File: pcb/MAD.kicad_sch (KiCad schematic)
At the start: 48 parts, among them J1 Conn_01x06_Pin, J2 Conn_01x06_Socket, Q1 AO3416A, Q10 AO3419A, Q11 AO3416A, Q12 AO3416A, Q2 AO3419A, Q3 AO3416A, Q4 AO3419A, Q5 AO3416A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

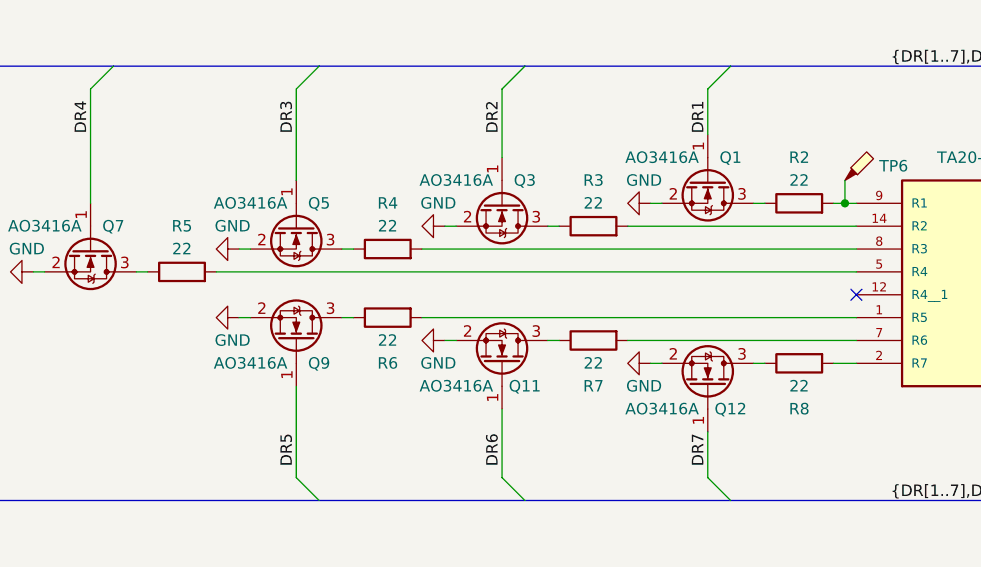
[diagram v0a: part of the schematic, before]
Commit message: Optimize resistor values
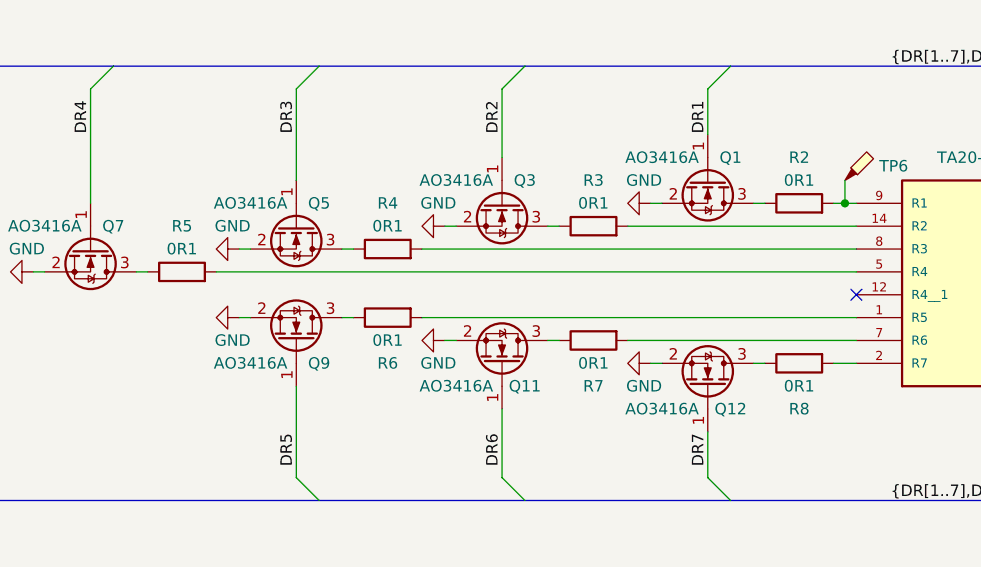
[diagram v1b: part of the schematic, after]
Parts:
- R2, R3, R4, R5, R6, R7, R8: value 22 -> 0R1
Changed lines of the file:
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@@
       (effects (font (size 1.27 1.27)))
     )
-    (property "Value" "22" (at 196.85 114.3 90)
+    (property "Value" "0R1" (at 196.85 114.3 90)
       (effects (font (size 1.27 1.27)))
     )
@@
       (effects (font (size 1.27 1.27)))
     )
-    (property "Value" "22" (at 173.99 111.76 90)
+    (property "Value" "0R1" (at 173.99 111.76 90)
       (effects (font (size 1.27 1.27)))
     )
@@
       (effects (font (size 1.27 1.27)))
     )
-    (property "Value" "22" (at 196.85 91.44 90)
+    (property "Value" "0R1" (at 196.85 91.44 90)
       (effects (font (size 1.27 1.27)))
     )
@@
       (effects (font (size 1.27 1.27)))
     )
-    (property "Value" "22" (at 151.13 109.22 90)
+    (property "Value" "0R1" (at 151.13 109.22 90)
       (effects (font (size 1.27 1.27)))
     )
@@
       (effects (font (size 1.27 1.27)))
     )
-    (property "Value" "22" (at 128.27 99.06 90)
+    (property "Value" "0R1" (at 128.27 99.06 90)
       (effects (font (size 1.27 1.27)))
     )
@@
       (effects (font (size 1.27 1.27)))
     )
-    (property "Value" "22" (at 151.13 96.52 90)
+    (property "Value" "0R1" (at 151.13 96.52 90)
       (effects (font (size 1.27 1.27)))
     )
@@
       (effects (font (size 1.27 1.27)))
     )
-    (property "Value" "22" (at 173.99 93.98 90)
-      (effects (font (size 1.27 1.27)))
-    )
+    (property "Value" "0R1" (at 173.99 93.98 90)
+      (effects (font (size 1.27 1.27)))
+    )

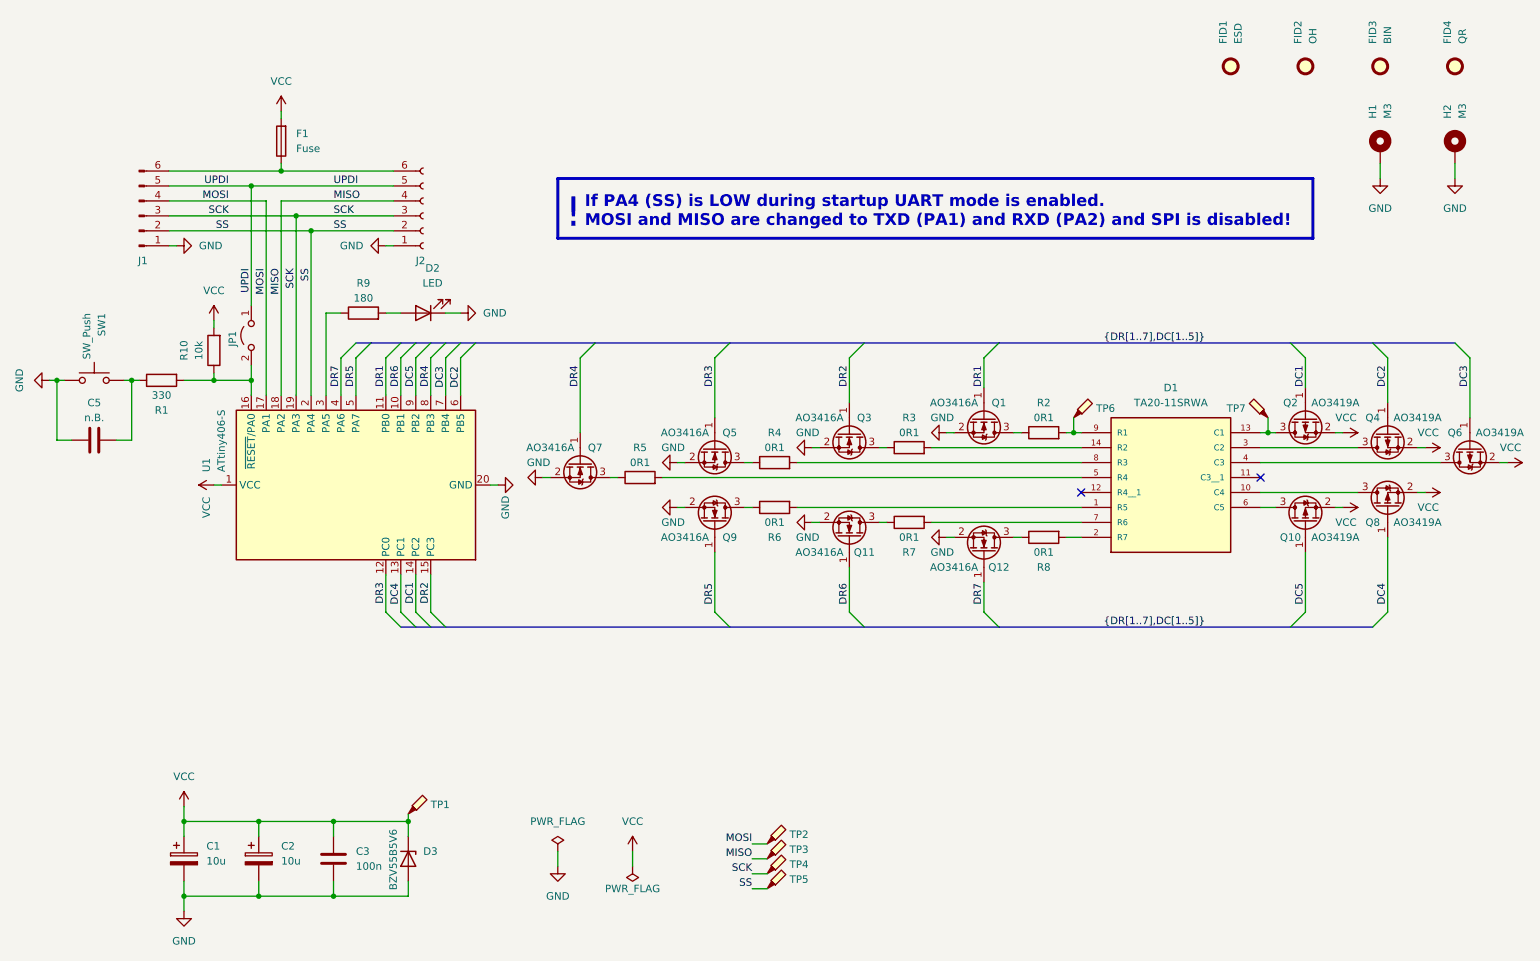
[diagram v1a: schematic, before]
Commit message: Change SPI-Bus names
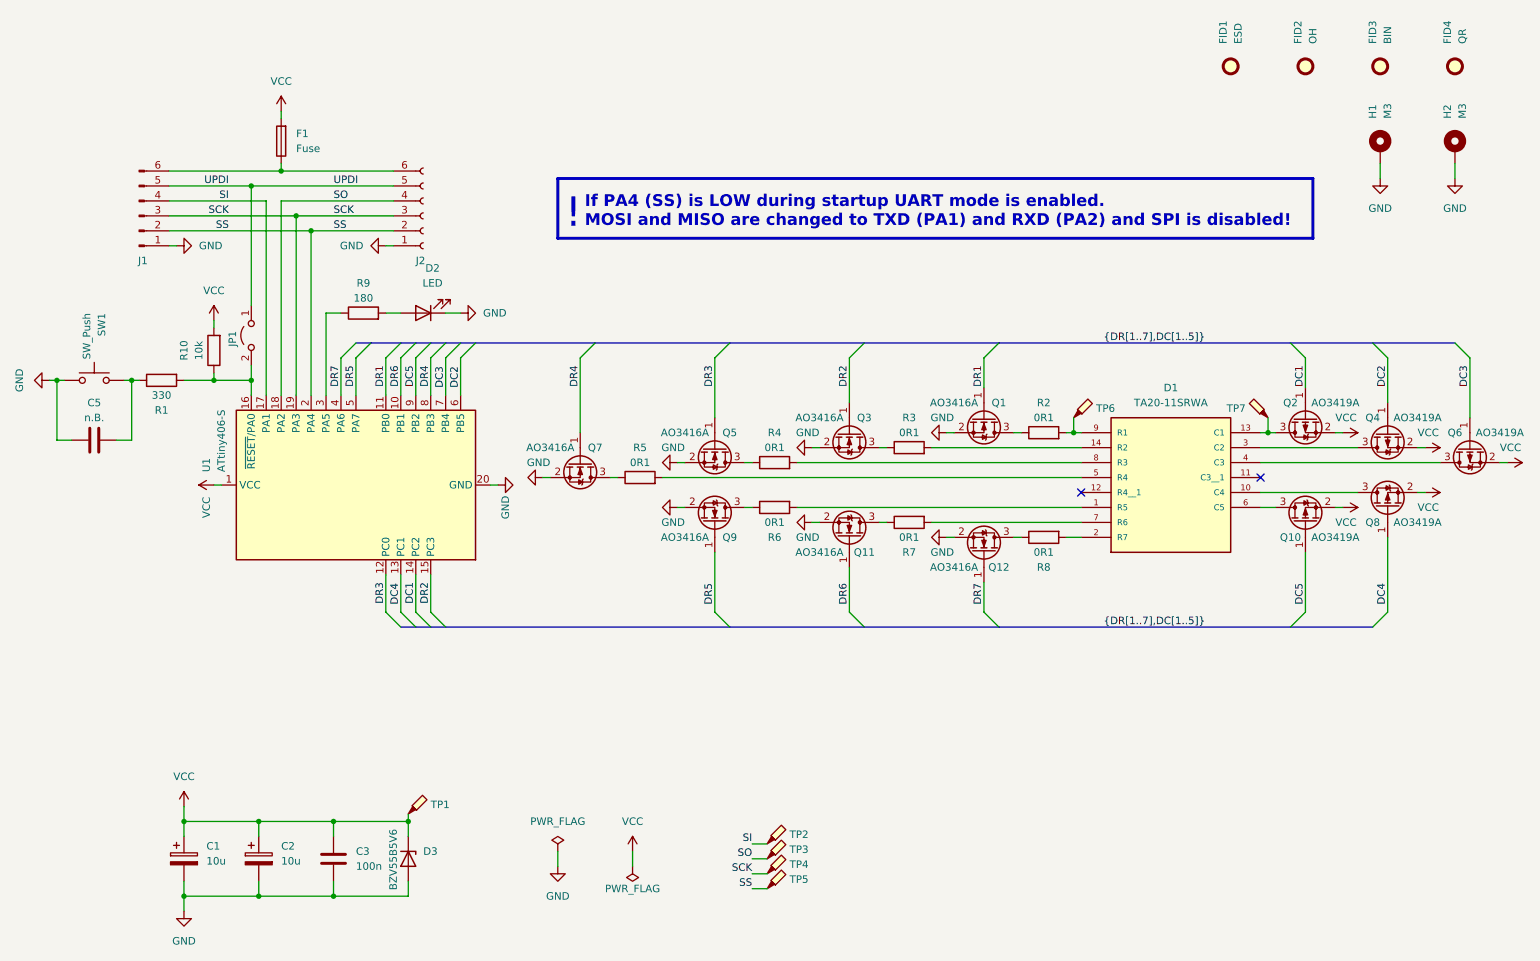
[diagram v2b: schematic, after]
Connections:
- net MISO renamed SO
- net MOSI renamed SI
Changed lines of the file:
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@@
     (effects (font (size 1.27 1.27)) (justify left bottom))
   )
-  (label "MOSI" (at 147.32 163.83 180) (fields_autoplaced)
+  (label "SI" (at 147.32 163.83 180) (fields_autoplaced)
     (effects (font (size 1.27 1.27)) (justify right bottom))
   )
   (label "DR6" (at 87.63 82.55 270) (fields_autoplaced)
-    (effects (font (size 1.27 1.27)) (justify right bottom))
-  )
-  (label "MOSI" (at 64.77 66.04 270) (fields_autoplaced)
     (effects (font (size 1.27 1.27)) (justify right bottom))
   )
@@
     (effects (font (size 1.27 1.27)) (justify left bottom))
   )
-  (label "MISO" (at 76.2 54.61 0) (fields_autoplaced)
+  (label "SO" (at 76.2 54.61 0) (fields_autoplaced)
     (effects (font (size 1.27 1.27)) (justify left bottom))
   )
@@
     (effects (font (size 1.27 1.27)) (justify right bottom))
   )
-  (label "MISO" (at 147.32 166.37 180) (fields_autoplaced)
+  (label "SO" (at 147.32 166.37 180) (fields_autoplaced)
     (effects (font (size 1.27 1.27)) (justify right bottom))
   )
@@
     (effects (font (size 1.27 1.27)) (justify left bottom))
   )
-  (label "SS" (at 72.39 66.04 270) (fields_autoplaced)
-    (effects (font (size 1.27 1.27)) (justify right bottom))
-  )
   (label "DC1" (at 90.17 119.38 270) (fields_autoplaced)
     (effects (font (size 1.27 1.27)) (justify right bottom))
@@
     (effects (font (size 1.27 1.27)) (justify left bottom))
   )
-  (label "UPDI" (at 62.23 66.04 270) (fields_autoplaced)
-    (effects (font (size 1.27 1.27)) (justify right bottom))
-  )
   (label "DR7" (at 186.69 123.19 90) (fields_autoplaced)
     (effects (font (size 1.27 1.27)) (justify left bottom))
-  )
-  (label "SCK" (at 69.85 66.04 270) (fields_autoplaced)
-    (effects (font (size 1.27 1.27)) (justify right bottom))
   )
   (label "DR3" (at 140.97 82.55 270) (fields_autoplaced)
     (effects (font (size 1.27 1.27)) (justify right bottom))
   )
-  (label "MOSI" (at 58.42 54.61 180) (fields_autoplaced)
+  (label "SI" (at 58.42 54.61 180) (fields_autoplaced)
     (effects (font (size 1.27 1.27)) (justify right bottom))
   )
@@
     (effects (font (size 1.27 1.27)) (justify right bottom))
   )
-  (label "MISO" (at 67.31 66.04 270) (fields_autoplaced)
-    (effects (font (size 1.27 1.27)) (justify right bottom))
-  )

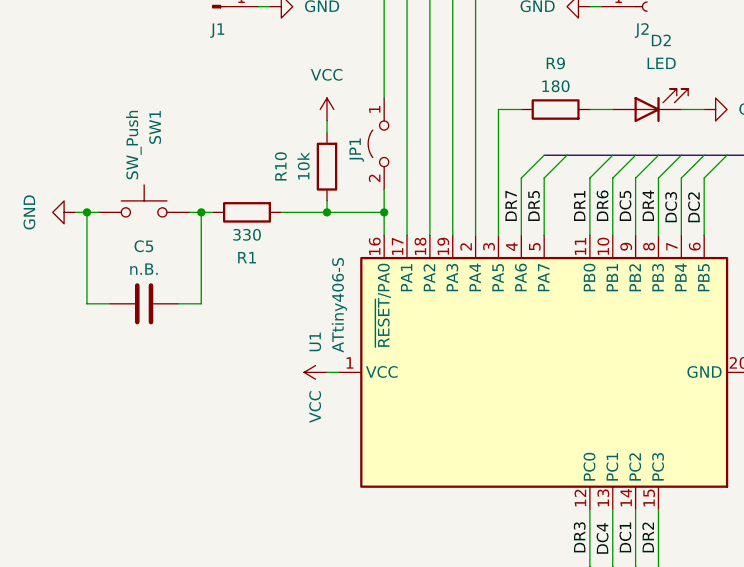
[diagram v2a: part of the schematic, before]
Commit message: Add ATtiny __06 to design
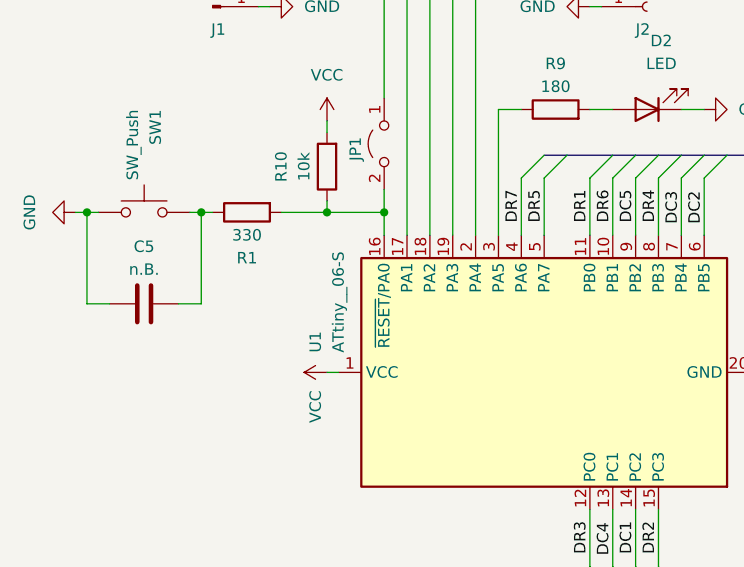
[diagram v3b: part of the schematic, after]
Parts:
- U1: value ATtiny406-S -> ATtiny__06-S; VendorId 103335 -> 103335,103450
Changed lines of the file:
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@@
       (effects (font (size 1.27 1.27)) (justify left))
     )
-    (property "Value" "ATtiny406-S" (at 57.15 100.6759 0)
+    (property "Value" "ATtiny__06-S" (at 57.15 100.6759 0)
       (effects (font (size 1.27 1.27)) (justify left))
     )
@@
       (effects (font (size 1.27 1.27)) hide)
     )
-    (property "VendorId" "103335" (at 80.01 102.87 0)
+    (property "VendorId" "103335,103450" (at 80.01 102.87 0)
       (effects (font (size 1.27 1.27)) hide)
     )

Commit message: Fix number in partlist
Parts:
- R2, R3, R4, R5, R6, R7, R8: VendorId 102919 -> 102901
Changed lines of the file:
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@@
       (effects (font (size 1.27 1.27)) hide)
     )
-    (property "VendorId" "102919" (at 196.85 111.76 0)
+    (property "VendorId" "102901" (at 196.85 111.76 0)
       (effects (font (size 1.27 1.27)) hide)
     )
@@
       (effects (font (size 1.27 1.27)) hide)
     )
-    (property "VendorId" "102919" (at 173.99 109.22 0)
+    (property "VendorId" "102901" (at 173.99 109.22 0)
       (effects (font (size 1.27 1.27)) hide)
     )
@@
       (effects (font (size 1.27 1.27)) hide)
     )
-    (property "VendorId" "102919" (at 196.85 93.98 0)
+    (property "VendorId" "102901" (at 196.85 93.98 0)
       (effects (font (size 1.27 1.27)) hide)
     )
@@
       (effects (font (size 1.27 1.27)) hide)
     )
-    (property "VendorId" "102919" (at 151.13 106.68 0)
+    (property "VendorId" "102901" (at 151.13 106.68 0)
       (effects (font (size 1.27 1.27)) hide)
     )
@@
       (effects (font (size 1.27 1.27)) hide)
     )
-    (property "VendorId" "102919" (at 128.27 101.6 0)
+    (property "VendorId" "102901" (at 128.27 101.6 0)
       (effects (font (size 1.27 1.27)) hide)
     )
@@
       (effects (font (size 1.27 1.27)) hide)
     )
-    (property "VendorId" "102919" (at 151.13 99.06 0)
+    (property "VendorId" "102901" (at 151.13 99.06 0)
       (effects (font (size 1.27 1.27)) hide)
     )
@@
       (effects (font (size 1.27 1.27)) hide)
     )
-    (property "VendorId" "102919" (at 173.99 96.52 0)
-      (effects (font (size 1.27 1.27)) hide)
-    )
+    (property "VendorId" "102901" (at 173.99 96.52 0)
+      (effects (font (size 1.27 1.27)) hide)
+    )

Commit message: Add mounting screw
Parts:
- H1, H2: VendorId 101017, 101382 -> 101017, 101018, 101382
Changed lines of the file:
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@@
       (effects (font (size 1.27 1.27)) hide)
     )
-    (property "VendorId" "101017, 101382" (at 254 45.72 0)
+    (property "VendorId" "101017, 101018, 101382" (at 254 45.72 0)
       (effects (font (size 1.27 1.27)) hide)
     )
@@
       (effects (font (size 1.27 1.27)) hide)
     )
-    (property "VendorId" "101017, 101382" (at 266.7 45.72 0)
-      (effects (font (size 1.27 1.27)) hide)
-    )
+    (property "VendorId" "101017, 101018, 101382" (at 266.7 45.72 0)
+      (effects (font (size 1.27 1.27)) hide)
+    )

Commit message: Optimize current consumption
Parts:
- R2, R3, R4, R5, R6, R7, R8: value 0R1 -> 15; VendorId 102901 -> 102916
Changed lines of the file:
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@@
       (effects (font (size 1.27 1.27)))
     )
-    (property "Value" "0R1" (at 196.85 114.3 90)
+    (property "Value" "15" (at 196.85 114.3 90)
       (effects (font (size 1.27 1.27)))
     )
@@
       (effects (font (size 1.27 1.27)) hide)
     )
-    (property "VendorId" "102901" (at 196.85 111.76 0)
+    (property "VendorId" "102916" (at 196.85 111.76 0)
       (effects (font (size 1.27 1.27)) hide)
     )
@@
       (effects (font (size 1.27 1.27)))
     )
-    (property "Value" "0R1" (at 173.99 111.76 90)
+    (property "Value" "15" (at 173.99 111.76 90)
       (effects (font (size 1.27 1.27)))
     )
@@
       (effects (font (size 1.27 1.27)) hide)
     )
-    (property "VendorId" "102901" (at 173.99 109.22 0)
+    (property "VendorId" "102916" (at 173.99 109.22 0)
       (effects (font (size 1.27 1.27)) hide)
     )
@@
       (effects (font (size 1.27 1.27)))
     )
-    (property "Value" "0R1" (at 196.85 91.44 90)
+    (property "Value" "15" (at 196.85 91.44 90)
       (effects (font (size 1.27 1.27)))
     )
@@
       (effects (font (size 1.27 1.27)) hide)
     )
-    (property "VendorId" "102901" (at 196.85 93.98 0)
+    (property "VendorId" "102916" (at 196.85 93.98 0)
       (effects (font (size 1.27 1.27)) hide)
     )
@@
       (effects (font (size 1.27 1.27)))
     )
-    (property "Value" "0R1" (at 151.13 109.22 90)
+    (property "Value" "15" (at 151.13 109.22 90)
       (effects (font (size 1.27 1.27)))
     )
@@
       (effects (font (size 1.27 1.27)) hide)
     )
-    (property "VendorId" "102901" (at 151.13 106.68 0)
+    (property "VendorId" "102916" (at 151.13 106.68 0)
       (effects (font (size 1.27 1.27)) hide)
     )
@@
       (effects (font (size 1.27 1.27)))
     )
-    (property "Value" "0R1" (at 128.27 99.06 90)
+    (property "Value" "15" (at 128.27 99.06 90)
       (effects (font (size 1.27 1.27)))
     )
@@
       (effects (font (size 1.27 1.27)) hide)
     )
-    (property "VendorId" "102901" (at 128.27 101.6 0)
+    (property "VendorId" "102916" (at 128.27 101.6 0)
       (effects (font (size 1.27 1.27)) hide)
     )
@@
       (effects (font (size 1.27 1.27)))
     )
-    (property "Value" "0R1" (at 151.13 96.52 90)
+    (property "Value" "15" (at 151.13 96.52 90)
       (effects (font (size 1.27 1.27)))
     )
@@
       (effects (font (size 1.27 1.27)) hide)
     )
-    (property "VendorId" "102901" (at 151.13 99.06 0)
+    (property "VendorId" "102916" (at 151.13 99.06 0)
       (effects (font (size 1.27 1.27)) hide)
     )
@@
       (effects (font (size 1.27 1.27)))
     )
-    (property "Value" "0R1" (at 173.99 93.98 90)
+    (property "Value" "15" (at 173.99 93.98 90)
       (effects (font (size 1.27 1.27)))
     )
@@
       (effects (font (size 1.27 1.27)) hide)
     )
-    (property "VendorId" "102901" (at 173.99 96.52 0)
-      (effects (font (size 1.27 1.27)) hide)
-    )
+    (property "VendorId" "102916" (at 173.99 96.52 0)
+      (effects (font (size 1.27 1.27)) hide)
+    )
